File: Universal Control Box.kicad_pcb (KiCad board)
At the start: 2 copper layers, 168.2 x 98.8 mm, 88 parts, among them J101 Conn_01x06, J102 Conn_01x07, J103 USB_C_Receptacle_USB2.0, U101 ESP32-WROOM-32, U102 PCF8575DBR (PCF1), U103 XC6220B331MR-G, U201 PEC11H-4025F-S0016, U202 PEC11H-4025F-S0016

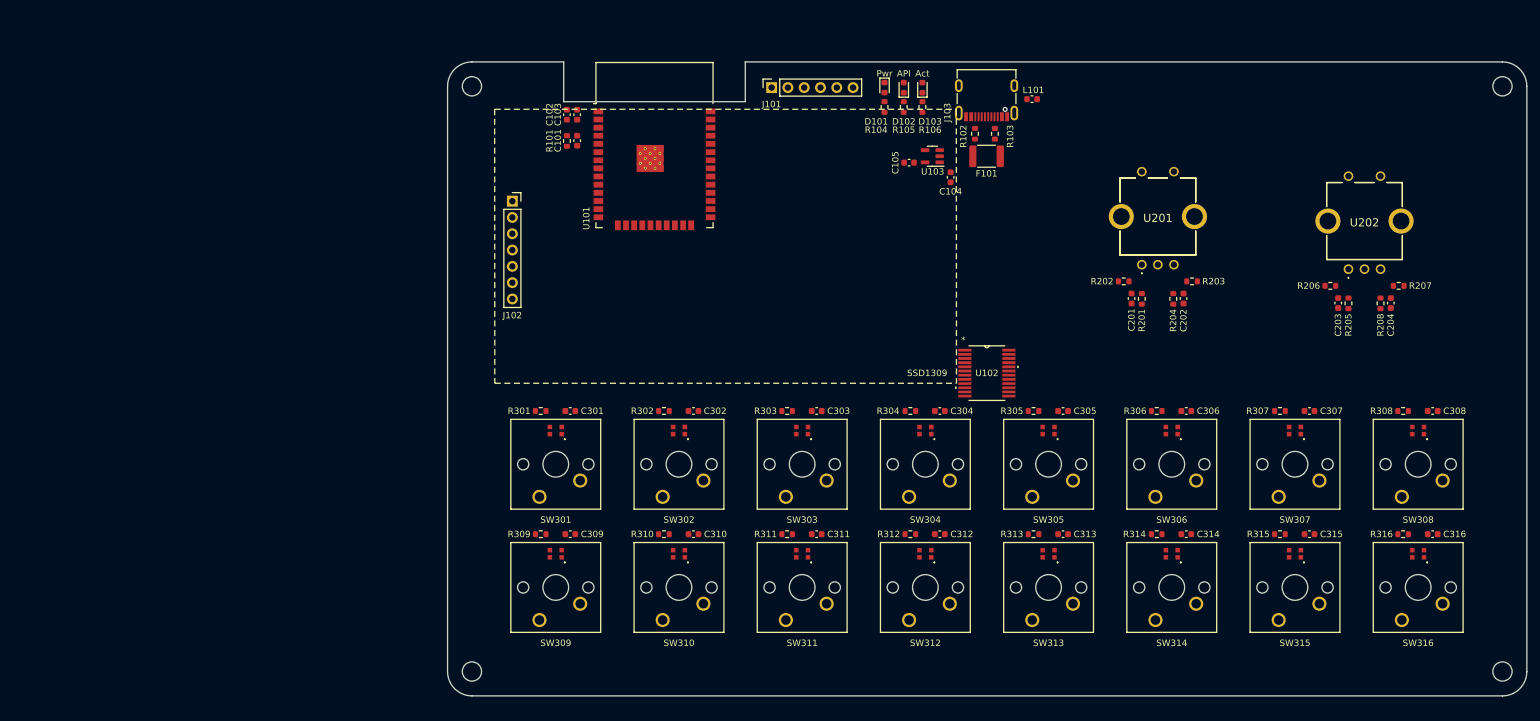
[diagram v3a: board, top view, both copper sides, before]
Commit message: Added GND & other stuff
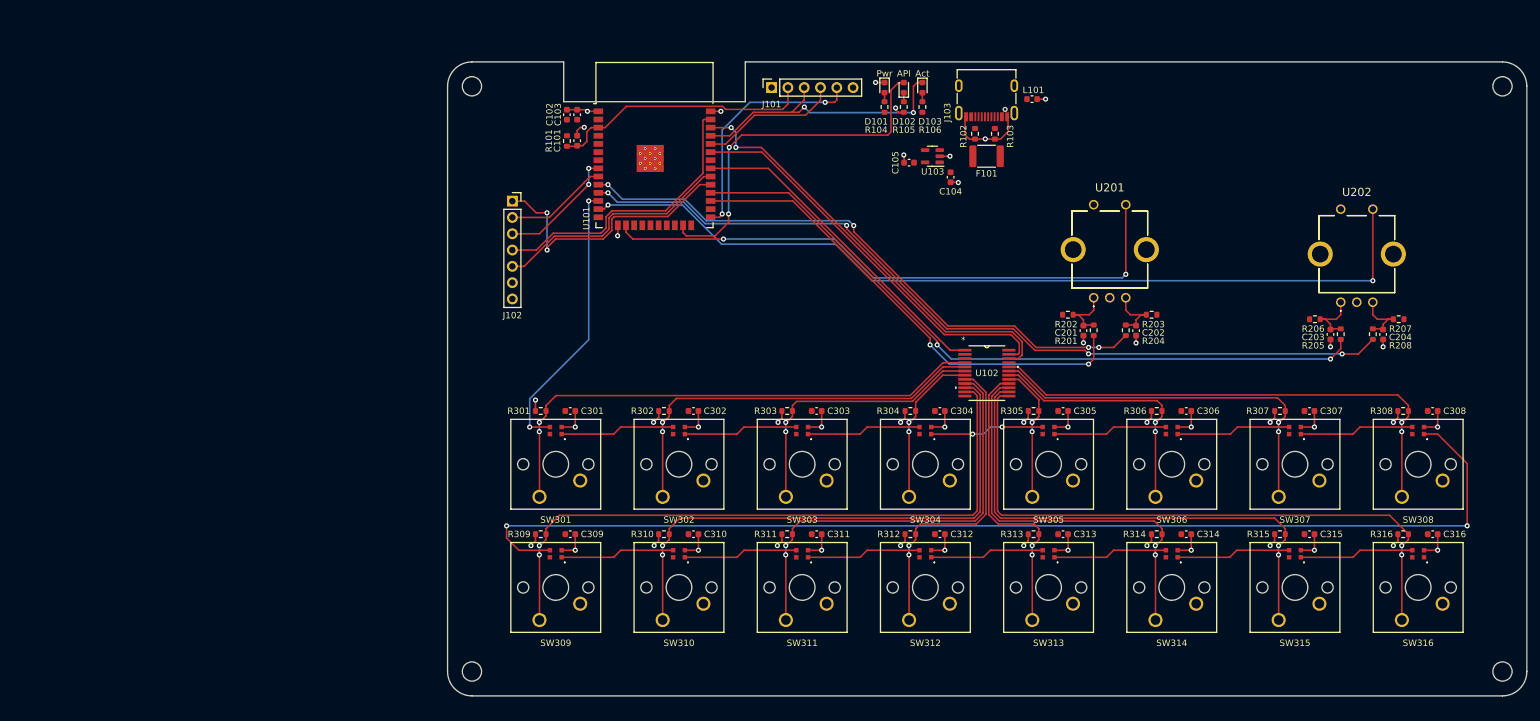
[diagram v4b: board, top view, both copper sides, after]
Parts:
- moved R202 10.1 mm to (179.4, 66.3)
- moved C201 9.01 mm to (181.8, 68.8)
- moved R201 8.96 mm to (183.4, 68.7)
- moved C202 8.93 mm to (190.0, 68.8)
- moved R204 8.88 mm to (188.4, 68.7)
- moved R203 8.17 mm to (192.4, 66.3)
- moved R206 5.73 mm to (217.9, 67.0)
- moved U201 5.42 mm to (185.9, 56.4)
- moved R207 5.20 mm to (230.9, 67.0)
- moved C203 5.04 mm to (220.3, 69.4)
- moved C204 5.04 mm to (228.5, 69.4)
- moved R205 4.95 mm to (221.9, 69.3)
- moved R208 4.95 mm to (226.9, 69.3)
- moved U202 2.47 mm to (224.4, 57.1)
- turned C101 to 90 degrees
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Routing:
- net Net-(SW308-DOUT): track 0.00 -> 177.5 mm, vias 0 -> 2
- net GND: track 0.00 -> 143.2 mm, vias 0 -> 47
- net /Rotary Encoders/SW_RSW2: track 0.00 -> 137.0 mm, vias 0 -> 2
- net /Rotary Encoders/B_RSW2: track 0.00 -> 132.3 mm, vias 0 -> 4
- net /Rotary Encoders/A_RSW2: track 0.00 -> 111.4 mm, vias 0 -> 2
- net /KeyCaps/SW9: track 0.00 -> 103.2 mm, vias 0 -> 2
- net /KeyCaps/SW16: track 0.00 -> 98.9 mm, vias 0 -> 2
- net /Rotary Encoders/B_RSW1: track 0.00 -> 94.0 mm, vias 0 -> 4
- net /Rotary Encoders/SW_RSW1: track 0.00 -> 93.0 mm, vias 0 -> 2
- net /KeyCaps/SW10: track 0.00 -> 85.4 mm, vias 0 -> 2
- net /KeyCaps/SW1: track 0.00 -> 82.7 mm, vias 0 -> 2
- net /KeyCaps/SW15: track 0.00 -> 81.6 mm, vias 0 -> 2
- net /KeyCaps/SW8: track 0.00 -> 79.5 mm, vias 0 -> 2
- net /Rotary Encoders/A_RSW1: track 0.00 -> 74.8 mm, vias 0 -> 2
- net /I2C_SCL: track 0.00 -> 68.1 mm, vias 0 -> 2
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- added copper zone on In1.Cu, net GND
- added copper zone on In2.Cu, net GND
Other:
- copper layers 2 -> 4

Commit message: Added remaining traces
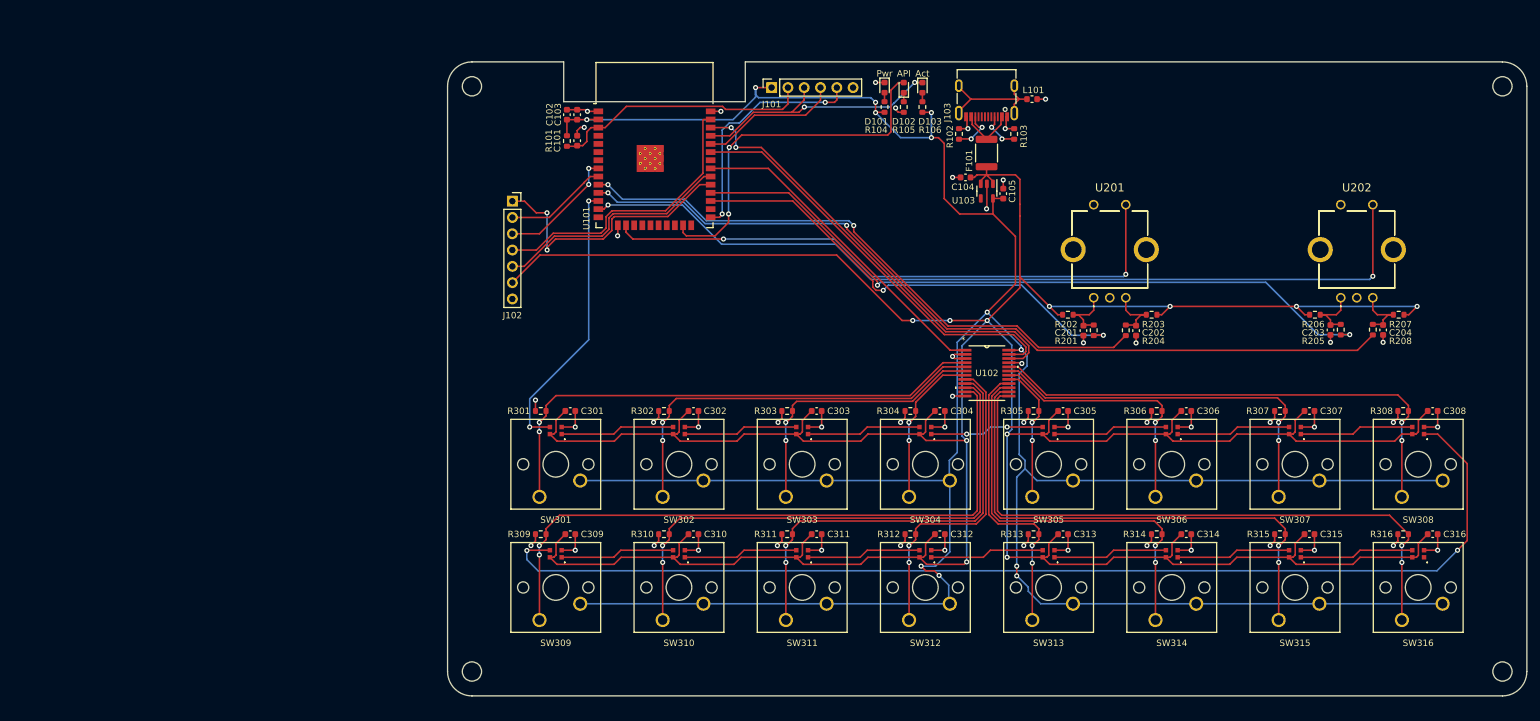
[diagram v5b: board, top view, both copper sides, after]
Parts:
- moved C105 15.4 mm to (169.3, 47.4), turned to 90 degrees
- moved U103 10.1 mm to (166.8, 47.0), turned to -90 degrees
- moved R103 3.00 mm to (171.0, 38.1), turned to -90 degrees
- moved R102 2.50 mm to (162.4, 38.1), turned to 90 degrees
- moved C104 2.33 mm to (163.4, 44.9), turned to 0 degrees
- moved C203 0.70 mm to (220.3, 68.7)
- moved C204 0.70 mm to (228.5, 68.7)
- moved R205 0.70 mm to (221.9, 68.6)
- moved R206 0.70 mm to (217.9, 66.3)
- moved R207 0.70 mm to (230.9, 66.3)
- moved R208 0.70 mm to (226.9, 68.6)
- moved U202 0.70 mm to (224.4, 56.4)
- moved F101 0.50 mm to (166.7, 41.1), turned to -90 degrees
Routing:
- net +5V: track 0.00 -> 617.0 mm, vias 0 -> 11
- net +3.3V: track 0.00 -> 470.7 mm, vias 0 -> 12
- net Net-(J103-SHIELD): track 0.00 -> 19.5 mm
- net Net-(F101-Pad1): track 0.00 -> 9.43 mm
- net Net-(J103-CC2): track 0.00 -> 6.76 mm, vias 0 -> 2
- net Net-(J103-CC1): track 0.00 -> 6.23 mm, vias 0 -> 2
- net GND: track 143.2 -> 147.8 mm, vias 47 -> 51
- net /ESP_TX: track 44.2 -> 41.1 mm
- net Net-(SW308-DOUT): track 177.5 -> 174.9 mm
- net /Rotary Encoders/A_RSW1: track 74.8 -> 72.6 mm
- net /I2C_SDA: track 63.7 -> 65.3 mm
- net /I2C_SCL: track 68.1 -> 69.6 mm
- net /Rotary Encoders/B_RSW2: track 132.3 -> 132.2 mm, vias 4 -> 2
- net /Rotary Encoders/B_RSW1: vias 4 -> 2

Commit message: Updated designs to meet feedback
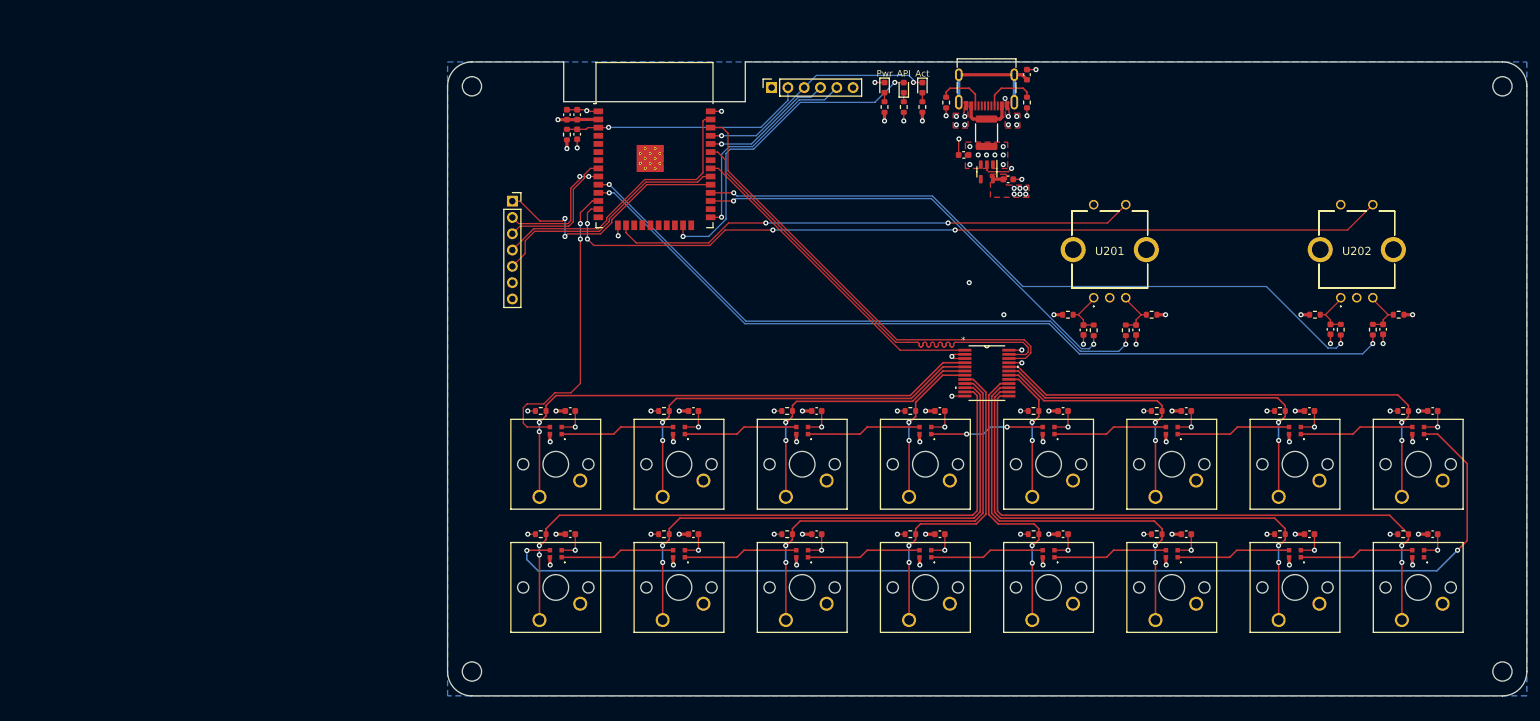
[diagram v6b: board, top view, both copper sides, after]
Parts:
- moved R102 5.29 mm to (160.4, 33.2), turned to -90 degrees
- moved R103 5.29 mm to (173.0, 33.2), turned to 90 degrees
- moved L101 3.89 mm to (173.0, 28.9), turned to -90 degrees
- moved C104 3.51 mm to (163.1, 41.4)
- moved F101 3.16 mm to (166.7, 37.9)
- moved U103 3.00 mm to (166.8, 44.0)
- moved C105 2.36 mm to (170.1, 45.2), turned to 0 degrees
- moved J103 1.70 mm to (166.7, 32.6)
- moved C101 1.00 mm to (102.9, 38.2), turned to -90 degrees
- moved R101 1.00 mm to (101.3, 38.2), turned to 90 degrees
- moved C201 0.10 mm to (181.8, 68.7)
- moved C202 0.10 mm to (190.0, 68.7)
- moved C203 0.10 mm to (220.3, 68.6)
- moved C204 0.10 mm to (228.5, 68.6)
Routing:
- net +3.3V: track 470.7 -> 14.0 mm, vias 12 -> 11
- net +5V: track 617.0 -> 183.0 mm, vias 11 -> 46
- net GND: track 147.8 -> 132.7 mm, vias 51 -> 59
- net /Rotary Encoders/SW_RSW1: track 92.8 -> 82.2 mm
- net /I2C_SDA: track 65.3 -> 72.1 mm
- net /Rotary Encoders/SW_RSW2: track 137.1 -> 131.5 mm, vias 2 -> 4
- net /OLED_CS: track 42.9 -> 38.8 mm
- net /HA_STATUS: track 56.2 -> 52.1 mm
- net /OLED_DC: track 16.1 -> 20.0 mm, vias 0 -> 2
- net /LED_DATA: track 43.7 -> 47.4 mm
- net /ESP_TX: track 41.1 -> 37.6 mm
- net /IO0: track 36.9 -> 33.8 mm, vias 2 -> 1
- net /EN: track 41.0 -> 38.3 mm, vias 0 -> 1
- net /I2C_SCL: track 69.6 -> 72.3 mm, vias 2 -> 0
- net Net-(J103-CC1): track 6.23 -> 8.23 mm, vias 2 -> 0
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- added copper zone on F.Cu, net +3.3V
- added copper zone on In2.Cu, net +3.3V
- added copper zone on F.Cu, net +5V
- added copper zone on In1.Cu, net +5V
- added copper zone on In2.Cu, net +5V
- added copper zone on B.Cu, net GND
- added copper zone on F.Cu, net GND
- removed copper zone on In2.Cu, net GND

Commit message: Some improvements & added labeling
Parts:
- added REF**: KiCad-Logo2_5mm_SilkScreen, Symbol:KiCad-Logo2_5mm_SilkScreen, F.Cu at (137.4, 50.6)
- D101, D102, D103: footprint LED_SMD:LED_0603_1608Metric -> LED_SMD:LED_0805_2012Metric
- moved D102 68.1 mm to (86.1, 23.8)
- moved D103 68.1 mm to (89.0, 23.8)
- moved C203 68.1 mm to (152.6, 61.5)
- moved R205 68.1 mm to (154.2, 61.5)
- moved R208 68.1 mm to (159.2, 61.5)
- moved U202 68.1 mm to (156.7, 49.3)
- moved C101 68.1 mm to (35.2, 31.1)
- moved C103 68.1 mm to (35.2, 28.0)
- moved C104 68.1 mm to (95.4, 34.3)
- moved C201 68.1 mm to (114.1, 61.6)
- moved C304 68.1 mm to (91.7, 74.2)
- moved C307 68.1 mm to (149.3, 74.2)
- moved C312 68.1 mm to (91.7, 93.4)
- moved C315 68.1 mm to (149.3, 93.4)
- moved D101 68.1 mm to (83.1, 23.8)
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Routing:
- net /Rotary Encoders/SW_RSW2: track 131.5 -> 146.0 mm
- net /Rotary Encoders/SW_RSW1: track 82.2 -> 96.1 mm
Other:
- board text added: "Adam Brodack"
- board text added: "JLCJLCJLCJLC"
- board text added: "Universal Controller ${REVISION}"

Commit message: Fixed library links
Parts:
- removed REF**: KiCad-Logo2_5mm_SilkScreen, Symbol:KiCad-Logo2_5mm_SilkScreen
- F101: footprint Adam_Custom_Footprints:Fuse_1812_4532Metric -> footprints:Fuse_1812_4532Metric
- J102: footprint Adam_Custom_Footprints:PinSocket_1x07_P2.54mm_Vertical_SSD1309 -> footprints:PinSocket_1x07_P2.54mm_Vertical_SSD1309
- J103: footprint Josh_Custom_Footprints:USB_C_Receptable_918-418K2023S40001 -> footprints:USB_C_Receptable_918-418K2023S40001
- SW301, SW302, SW303, SW304, SW305, SW306, SW307, SW308, SW309, SW310, SW311, SW312, SW313, SW314, SW315, SW316: footprint Adam_Custom_Footprints:CherryMX_1.00u_PCB_WS2812B-2020 -> footprints:CherryMX_1.00u_PCB_WS2812B-2020
- U101: footprint Josh_Custom_Footprints:ESP32-WROOM-32 -> footprints:ESP32-WROOM-32
- U102: footprint Adam_Custom_Footprints:TexasInstruments_PCF8575DBR -> footprints:TexasInstruments_PCF8575DBR
- U201, U202: footprint Adam_Custom_Footprints:PEC11H4025FS0016 -> footprints:PEC11H4025FS0016
